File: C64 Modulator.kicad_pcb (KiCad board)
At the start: 2 copper layers, 63.5 x 63.4 mm, 40 parts, among them J10 , J11 , J12 , J13 , J14 , J2 8765, J3 4321, J4 AUD_RIGHT, J5 TRS_3.5mm, J6 RCA_PLUG, J7 , J8 , J9 , Q1 BC549, Q2 BC549, U1 LM7805

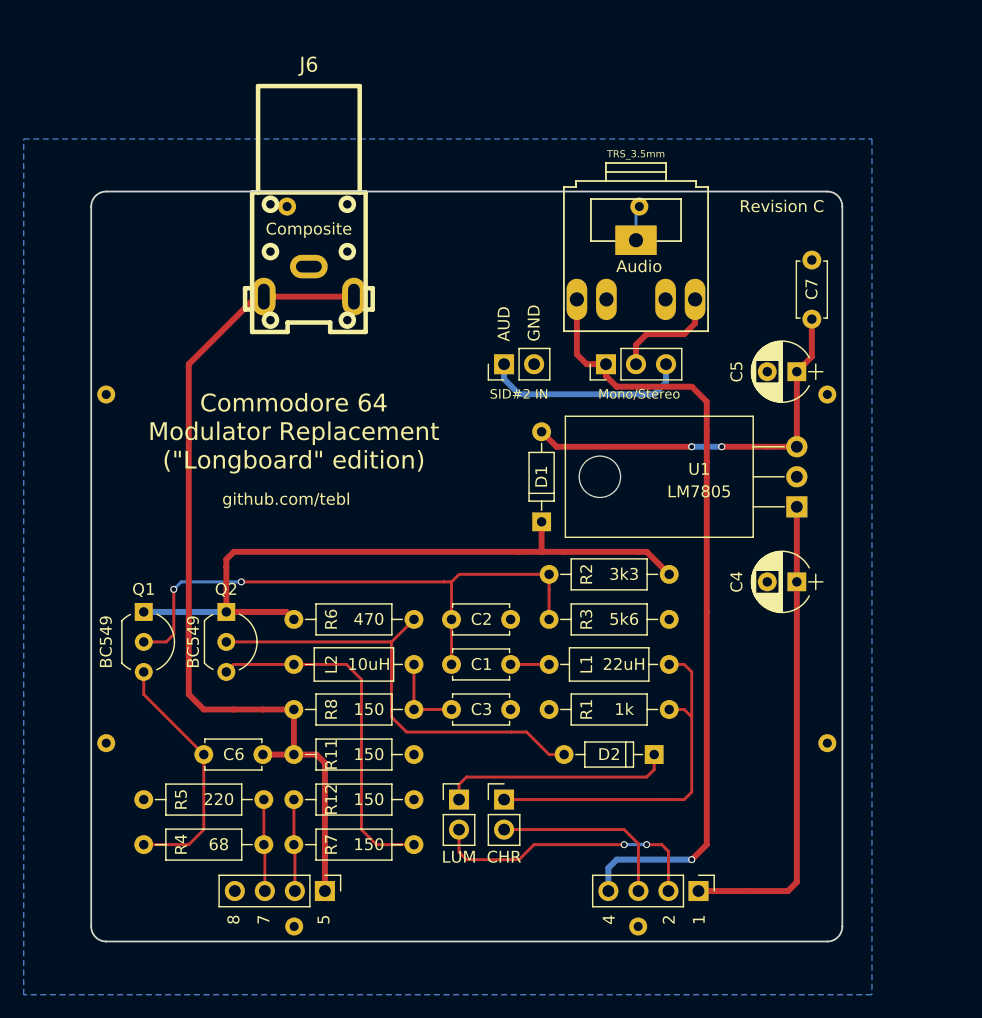
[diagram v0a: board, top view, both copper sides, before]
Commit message: Cleaned up library for new KiCad & started splitting Chroma/Luma/Comp
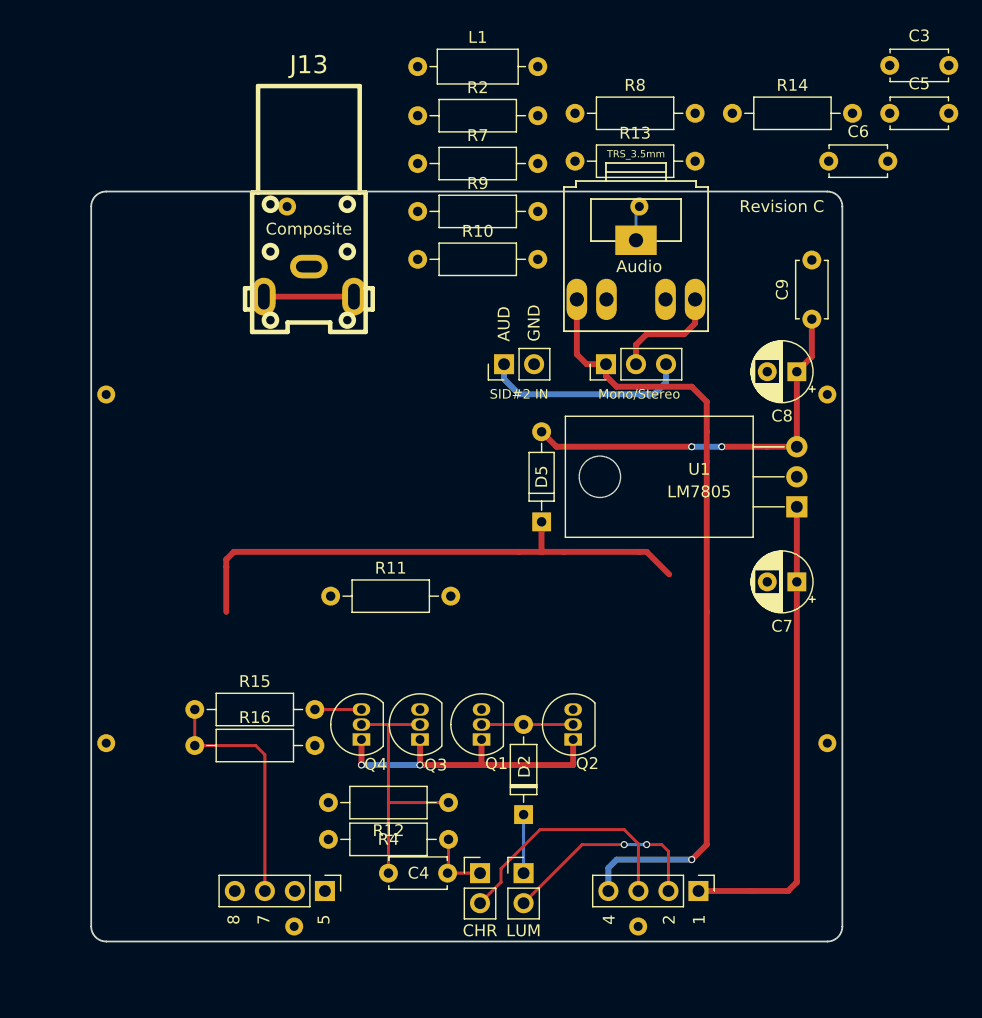
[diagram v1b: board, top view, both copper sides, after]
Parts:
- removed C1: 330pF, Capacitors_THT:C_Disc_D4.7mm_W2.5mm_P5.00mm
- removed C2: 150pF, Capacitors_THT:C_Disc_D4.7mm_W2.5mm_P5.00mm
- removed the JP3 at (153.7, 113.7)
- removed JP4: LUM, Pin_Headers:Pin_Header_Straight_1x02_Pitch2.54mm
- removed L2: 10uH, Inductors_THT:L_Axial_L6.6mm_D2.7mm_P10.16mm_Horizontal_Vishay_IM-2
- removed R1: 1k, Resistors_THT:R_Axial_DIN0207_L6.3mm_D2.5mm_P10.16mm_Horizontal
- removed R3: 5k6, Resistors_THT:R_Axial_DIN0207_L6.3mm_D2.5mm_P10.16mm_Horizontal
- removed R5: 220, Resistors_THT:R_Axial_DIN0207_L6.3mm_D2.5mm_P10.16mm_Horizontal
- removed R6: 470, Resistors_THT:R_Axial_DIN0207_L6.3mm_D2.5mm_P10.16mm_Horizontal
- added C4: 330pF, Capacitor_THT:C_Disc_D4.7mm_W2.5mm_P5.00mm, F.Cu at (143.9, 119.9)
- added C5: 150pF, Capacitor_THT:C_Disc_D4.7mm_W2.5mm_P5.00mm, F.Cu at (186.3, 55.6)
- added JP1: CHR, Connector_PinHeader_2.54mm:PinHeader_1x02_P2.54mm_Vertical, F.Cu at (151.6, 119.9)
- added JP2: LUM, Connector_PinHeader_2.54mm:PinHeader_1x02_P2.54mm_Vertical, F.Cu at (155.3, 119.9)
- added Q3: BC549, Package_TO_SOT_THT:TO-92_Inline, F.Cu at (146.6, 108.6)
- added Q4: BC549, Package_TO_SOT_THT:TO-92_Inline, F.Cu at (141.6, 108.6)
- added R10: 220, Resistor_THT:R_Axial_DIN0207_L6.3mm_D2.5mm_P10.16mm_Horizontal, F.Cu at (146.4, 68.0)
- added R13: 150, Resistor_THT:R_Axial_DIN0207_L6.3mm_D2.5mm_P10.16mm_Horizontal, F.Cu at (159.7, 59.7)
- added R14: 150, Resistor_THT:R_Axial_DIN0207_L6.3mm_D2.5mm_P10.16mm_Horizontal, F.Cu at (173.0, 55.6)
- added R15: 68, Resistor_THT:R_Axial_DIN0207_L6.3mm_D2.5mm_P10.16mm_Horizontal, F.Cu at (127.5, 106.0)
- added R16: 220, Resistor_THT:R_Axial_DIN0207_L6.3mm_D2.5mm_P10.16mm_Horizontal, F.Cu at (127.5, 109.1)
- added R9: 150, Resistor_THT:R_Axial_DIN0207_L6.3mm_D2.5mm_P10.16mm_Horizontal, F.Cu at (146.4, 63.9)
- C3, C6: footprint Capacitors_THT:C_Disc_D4.7mm_W2.5mm_P5.00mm -> Capacitor_THT:C_Disc_D4.7mm_W2.5mm_P5.00mm
- C7: renamed from C4; footprint Capacitors_THT:CP_Radial_D5.0mm_P2.50mm -> Capacitor_THT:CP_Radial_D5.0mm_P2.50mm
- C8: renamed from C5; footprint Capacitors_THT:CP_Radial_D5.0mm_P2.50mm -> Capacitor_THT:CP_Radial_D5.0mm_P2.50mm
- C9: renamed from C7; footprint Capacitors_THT:C_Disc_D4.7mm_W2.5mm_P5.00mm -> Capacitor_THT:C_Disc_D4.7mm_W2.5mm_P5.00mm
- D2: footprint Diodes_THT:D_DO-35_SOD27_P7.62mm_Horizontal -> Diode_THT:D_DO-35_SOD27_P7.62mm_Horizontal
- L1: value 22uH -> 10uH; footprint Inductors_THT:L_Axial_L6.6mm_D2.7mm_P10.16mm_Horizontal_Vishay_IM-2 -> Inductor_THT:L_Axial_L6.6mm_D2.7mm_P10.16mm_Horizontal_Vishay_IM-2
- Q1, Q2: footprint TO_SOT_Packages_THT:TO-92_Inline_Wide -> Package_TO_SOT_THT:TO-92_Inline
- R11: value 150 -> 3k3; footprint Resistors_THT:R_Axial_DIN0207_L6.3mm_D2.5mm_P10.16mm_Horizontal -> Resistor_THT:R_Axial_DIN0207_L6.3mm_D2.5mm_P10.16mm_Horizontal
- R12: value 150 -> 5k6; footprint Resistors_THT:R_Axial_DIN0207_L6.3mm_D2.5mm_P10.16mm_Horizontal -> Resistor_THT:R_Axial_DIN0207_L6.3mm_D2.5mm_P10.16mm_Horizontal
- R2: value 3k3 -> 470; footprint Resistors_THT:R_Axial_DIN0207_L6.3mm_D2.5mm_P10.16mm_Horizontal -> Resistor_THT:R_Axial_DIN0207_L6.3mm_D2.5mm_P10.16mm_Horizontal
- R4: value 68 -> 1k; footprint Resistors_THT:R_Axial_DIN0207_L6.3mm_D2.5mm_P10.16mm_Horizontal -> Resistor_THT:R_Axial_DIN0207_L6.3mm_D2.5mm_P10.16mm_Horizontal
- R7: footprint Resistors_THT:R_Axial_DIN0207_L6.3mm_D2.5mm_P10.16mm_Horizontal -> Resistor_THT:R_Axial_DIN0207_L6.3mm_D2.5mm_P10.16mm_Horizontal
- R8: value 150 -> 68; footprint Resistors_THT:R_Axial_DIN0207_L6.3mm_D2.5mm_P10.16mm_Horizontal -> Resistor_THT:R_Axial_DIN0207_L6.3mm_D2.5mm_P10.16mm_Horizontal
- moved C6 72.9 mm to (181.1, 59.7)
- moved C3 65.9 mm to (186.3, 51.6)
- moved R7 58.6 mm to (146.4, 59.9)
- moved R8 55.8 mm to (159.7, 55.6)
- moved L1 54.9 mm to (146.4, 51.7), turned to 0 degrees
- moved R2 40.4 mm to (146.4, 55.8)
- moved Q2 31.3 mm to (159.5, 108.6), turned to 90 degrees
- moved Q1 30.5 mm to (151.8, 108.6), turned to 90 degrees
- moved R4 15.6 mm to (149.0, 117.0)
- moved R11 13.8 mm to (139.0, 96.5)
- moved R12 13.1 mm to (149.0, 113.9), turned to 180 degrees
- moved D2 12.2 mm to (155.3, 114.9), turned to 90 degrees
- renumbered D1 to D5, J7 to J1, J3 to J10, J4 to J11, J5 to J12, J6 to J13, J8 to J2, J9 to J3, J10 to J4, J11 to J5, J12 to J6, J13 to J7, J14 to J8, J2 to J9, JP2 to JP3
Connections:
- L1 pad 1: CHROMA_IN -> Net-(C3-Pad1)
- L1 pad 2: Net-(C1-Pad2) -> Net-(L1-Pad2)
- Q1 pad 2: Net-(C1-Pad1) -> Net-(D2-Pad2)
- Q1 pad 3: Net-(C6-Pad1) -> Net-(Q1-Pad3)
- Q2 pad 3: Net-(L2-Pad2) -> Net-(L1-Pad2)
- R11 pad 1: COMPOSITE -> Net-(C4-Pad1)
- R11 pad 2: GND -> VCC
- R12 pad 1: LUMA_OUT -> Net-(C4-Pad1)
- R2 pad 1: Net-(C1-Pad1) -> VCC
- R2 pad 2: VCC -> Net-(D2-Pad2)
- R4 pad 1: CHROMA_OUT -> CHROMA_IN
- R4 pad 2: Net-(C6-Pad1) -> GND
- R7 pad 1: LUMA_OUT -> COMPOSITE
- R7 pad 2: Net-(L2-Pad2) -> Net-(C3-Pad1)
- R8 pad 1: COMPOSITE -> Net-(C6-Pad1)
- R8 pad 2: Net-(C3-Pad1) -> Net-(Q3-Pad3)
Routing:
- net COMPOSITE: track 73.9 -> 8.25 mm
- net Net-(C1-Pad1): track 49.7 -> 0.00 mm, vias 2 -> 0
- net Net-(D2-Pad2): track 38.9 -> 7.75 mm
- net Net-(L2-Pad2): track 29.9 -> 0.00 mm
- net CHROMA_IN: track 30.6 -> 5.64 mm
- net Net-(C4-Pad1): track 0.00 -> 22.6 mm
- net Net-(C6-Pad1): track 21.0 -> 0.00 mm
- net LUMA_IN: track 19.6 -> 4.95 mm
- net VCC: track 58.5 -> 71.8 mm, vias 0 -> 2
- net CHROMA_OUT: track 7.77 -> 20.8 mm
- net LUMA_OUT: track 7.77 -> 0.00 mm
- net Net-(C3-Pad1): track 6.98 -> 0.00 mm
- net Net-(J10-Pad2): track 24.1 -> 18.0 mm
- net Net-(J10-Pad3): track 15.9 -> 21.2 mm
- net Net-(Q4-Pad3): track 0.00 -> 3.94 mm
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- removed copper zone on B.Cu, net GND
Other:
- board text removed: "Commodore 64 Modulator Replacement ("Longboard" edition)"
- board text removed: "L1, C8, C9, D1 pads can be shorted, C2 & C3 can be left out."
- board text removed: "L2, C6, R8, R11 & RCA can be left out if composite video is not required."
- board text removed: "github.com/tebl"

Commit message: Completed double-buffering Chroma/Luma split & library cleanup
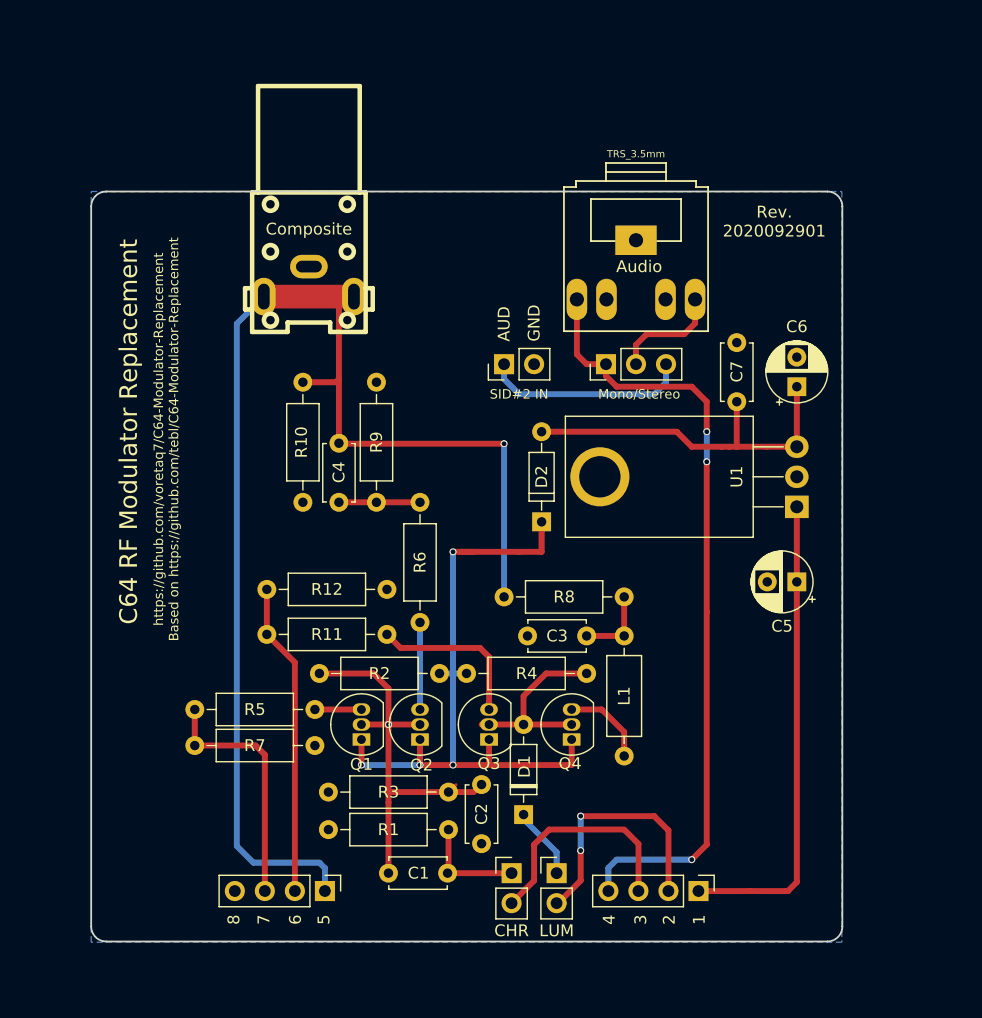
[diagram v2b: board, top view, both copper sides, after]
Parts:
- removed the J1 at (120.0, 79.4)
- removed the J2 at (135.9, 124.5)
- removed the J3 at (181.0, 109.4)
- removed the J4 at (168.9, 63.5)
- removed the J5 at (181.0, 79.4)
- removed J6, J7, J8: , anchors:anchor_circle
- C5: renamed from C7; value 10uF -> 22uF
- C6: renamed from C8; value 100uF -> 10uF
- J3: renamed from J11; footprint Pin_Headers:Pin_Header_Straight_1x02_Pitch2.54mm -> Connector_PinHeader_2.54mm:PinHeader_1x02_P2.54mm_Vertical
- U1: footprint TO_SOT_Packages_THT:TO-220-3_Horizontal -> Package_TO_SOT_THT:TO-220-3_Horizontal_TabDown
- moved C2 66.5 mm to (151.8, 112.4), turned to 270 degrees
- moved R12 56.3 mm to (133.6, 95.9)
- moved C3 54.6 mm to (160.7, 99.8), turned to 180 degrees
- moved L1 51.2 mm to (163.8, 99.8), turned to 270 degrees
- moved C4 50.5 mm to (139.7, 88.5), turned to 90 degrees
- moved R11 47.8 mm to (133.6, 99.7)
- moved R4 47.4 mm to (150.5, 103.0)
- moved R8 37.4 mm to (153.7, 96.5)
- moved R6 35.4 mm to (146.6, 88.5), turned to 270 degrees
- moved R9 20.8 mm to (142.9, 88.5), turned to 90 degrees
- moved R10 17.4 mm to (136.7, 78.4), turned to 270 degrees
- moved C7 9.44 mm to (173.4, 80.0)
- moved R2 6.61 mm to (138.0, 103.0)
- moved JP2 2.79 mm to (158.1, 119.9)
- moved JP1 2.67 mm to (154.3, 119.9)
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- renumbered C4 to C1, C5 to C2, C6 to C4, C9 to C7, D2 to D1, D5 to D2, J9 to J1, J10 to J2, J12 to J4, J13 to J5, Q4 to Q1, Q3 to Q2, Q1 to Q3, Q2 to Q4, R4 to R1, R9 to R10, R13 to R11, R14 to R12, R11 to R2, R12 to R3, R2 to R4, R15 to R5, R8 to R6, R16 to R7, R7 to R8, R10 to R9
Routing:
- net COMPOSITE: track 8.25 -> 109.5 mm, vias 0 -> 1
- net LUMA_OUT: track 0.00 -> 26.5 mm
- net Net-(Q3-Pad3): track 0.00 -> 14.8 mm
- net VCC: track 71.8 -> 57.7 mm, vias 2 -> 4
- net Net-(C1-Pad1): track 22.6 -> 36.0 mm, vias 0 -> 1
- net Net-(D1-Pad2): track 7.75 -> 17.3 mm
- net Net-(L1-Pad2): track 0.00 -> 8.27 mm
- net Net-(Q2-Pad3): track 0.00 -> 7.37 mm
- net Net-(C4-Pad1): track 0.00 -> 6.86 mm
- net Net-(C3-Pad1): track 0.00 -> 6.48 mm
- net Net-(J2-Pad2): track 18.0 -> 22.9 mm
- net CHROMA_IN: track 5.64 -> 9.13 mm
- net GND: track 2.97 -> 0.00 mm
- net Net-(C6-Pad1): track 33.4 -> 31.0 mm, vias 2 -> 0
- net Net-(J2-Pad3): track 21.2 -> 19.7 mm
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- added copper zone on B.Cu, net GND
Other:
- board text added: "3"
- board text added: "6"
- board text added: "C64 RF Modulator Replacement"
- board text added: "JLCJLCJLCJLC"
- board text added: "Rev. 2020092901"
- board text added: "https://github.com/voretaq7/C64-Modulator-Replacement Based on https://github.com/tebl/C64-Modulator-Replacement"
- board text removed: "Revision C"

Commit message: Minor PCB cleanup - Move Composite signal to top layer.
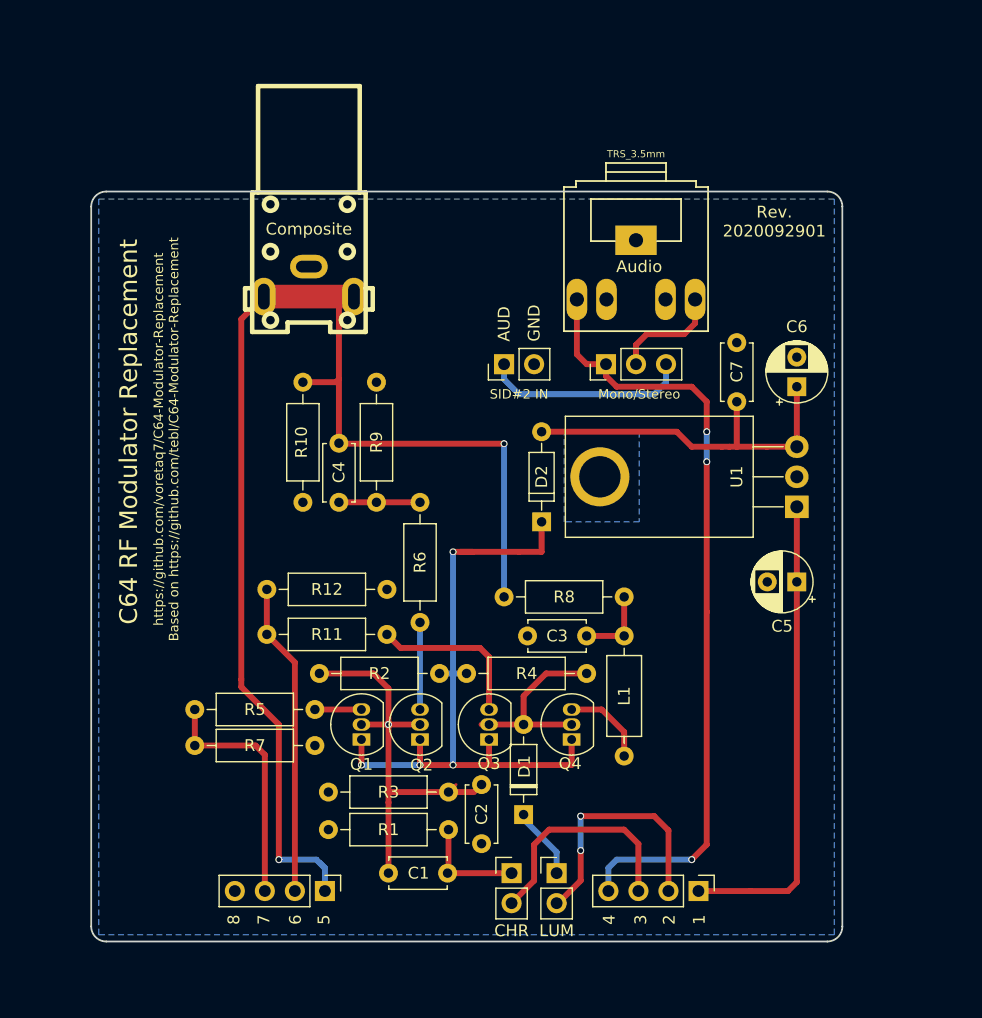
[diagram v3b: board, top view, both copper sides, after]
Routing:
- net COMPOSITE: track 109.5 -> 108.5 mm, vias 1 -> 2
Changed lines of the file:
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@@
     (thickness 1.6)
     (drawings 42)
-    (tracks 152)
+    (tracks 156)
     (zones 0)
     (modules 35)
@@
     (add_net "Net-(J2-Pad3)")
     (add_net "Net-(J3-Pad1)")
-    (add_net "Net-(J4-Pad3)")
-    (add_net "Net-(J4-Pad4)")
     (add_net "Net-(L1-Pad2)")
     (add_net "Net-(Q1-Pad3)")
@@
   (segment (start 138.049 118.999) (end 138.515 119.465) (width 0.5) (layer B.Cu) (net 4))
   (segment (start 138.515 119.465) (end 138.515 121.4) (width 0.5) (layer B.Cu) (net 4))
-  (segment (start 132.461 118.999) (end 138.049 118.999) (width 0.5) (layer B.Cu) (net 4))
-  (segment (start 131.064 117.602) (end 132.461 118.999) (width 0.5) (layer B.Cu) (net 4))
-  (segment (start 131.064 73.406) (end 131.064 117.602) (width 0.5) (layer B.Cu) (net 4))
-  (segment (start 133.35 71.12) (end 131.064 73.406) (width 0.5) (layer B.Cu) (net 4))
   (segment (start 140.97 71.12) (end 133.35 71.12) (width 2) (layer F.Cu) (net 4))
+  (segment (start 133.35 71.12) (end 131.445 73.025) (width 0.5) (layer F.Cu) (net 4))
+  (segment (start 131.445 73.025) (end 131.445 103.505) (width 0.5) (layer F.Cu) (net 4))
+  (segment (start 131.445 103.505) (end 131.445 104.14) (width 0.5) (layer F.Cu) (net 4))
+  (via (at 134.62 118.745) (size 0.6) (drill 0.4) (layers F.Cu B.Cu) (net 4))
+  (segment (start 134.62 107.315) (end 134.62 118.745) (width 0.5) (layer F.Cu) (net 4))
+  (segment (start 131.445 104.14) (end 134.62 107.315) (width 0.5) (layer F.Cu) (net 4))
+  (segment (start 134.62 118.745) (end 137.795 118.745) (width 0.5) (layer B.Cu) (net 4))
+  (segment (start 138.515 119.465) (end 137.795 118.745) (width 0.5) (layer B.Cu) (net 4))
   (via (at 141.605 110.744) (size 0.6) (drill 0.4) (layers F.Cu B.Cu) (net 5))
   (via (at 146.558 110.744) (size 0.6) (drill 0.4) (layers F.Cu B.Cu) (net 5))
@@
     (polygon
       (pts
-        (xy 182.245 125.73) (xy 118.745 125.73) (xy 118.745 62.23) (xy 182.245 62.23)
+        (xy 165.1 90.17) (xy 158.75 90.17) (xy 158.75 82.55) (xy 165.1 82.55)
       )
     )
+  )
+  (zone (net 1) (net_name GND) (layer B.Cu) (hatch edge 0.508)
+    (connect_pads (clearance 0.508))
+    (min_thickness 0.254)
+    (fill yes (arc_segments 32) (thermal_gap 0.508) (thermal_bridge_width 0.508))
+    (polygon
+      (pts
+        (xy 181.61 125.095) (xy 119.38 125.095) (xy 119.38 62.865) (xy 181.61 62.865)
+      )
+    )
